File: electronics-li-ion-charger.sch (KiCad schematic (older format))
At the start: 16 parts, among them J1 Conn_01x01_Male, J2 Conn_01x01_Male, J3 USB_B_Micro, J4 Conn_01x03_Male, U1 MCP73831-2-OT

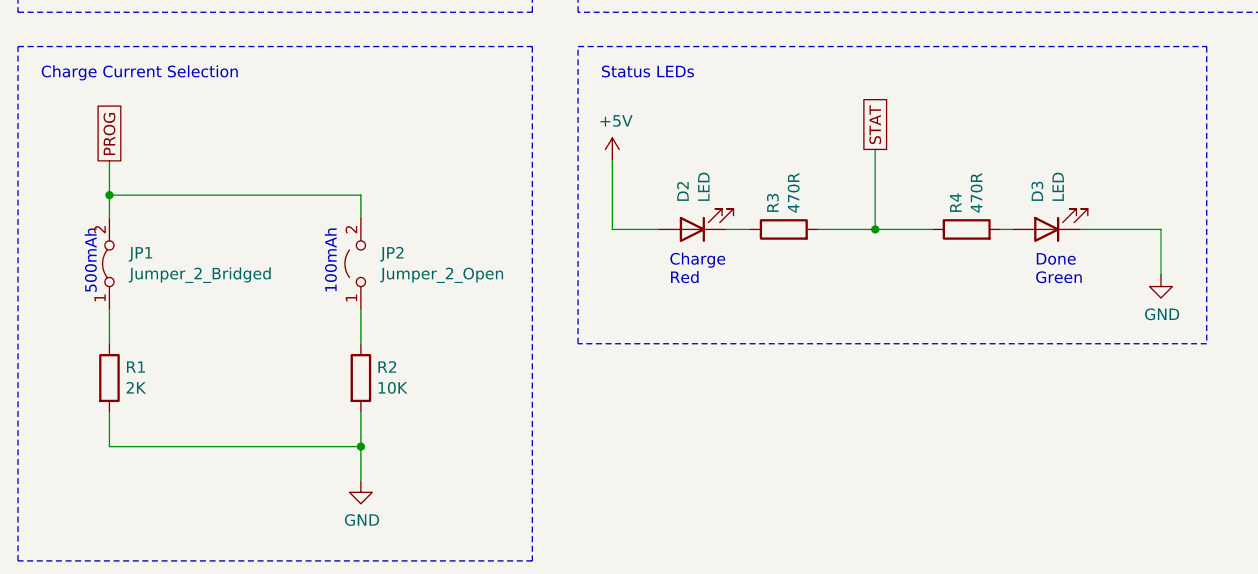
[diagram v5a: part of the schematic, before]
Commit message: Place components in PCB layout.
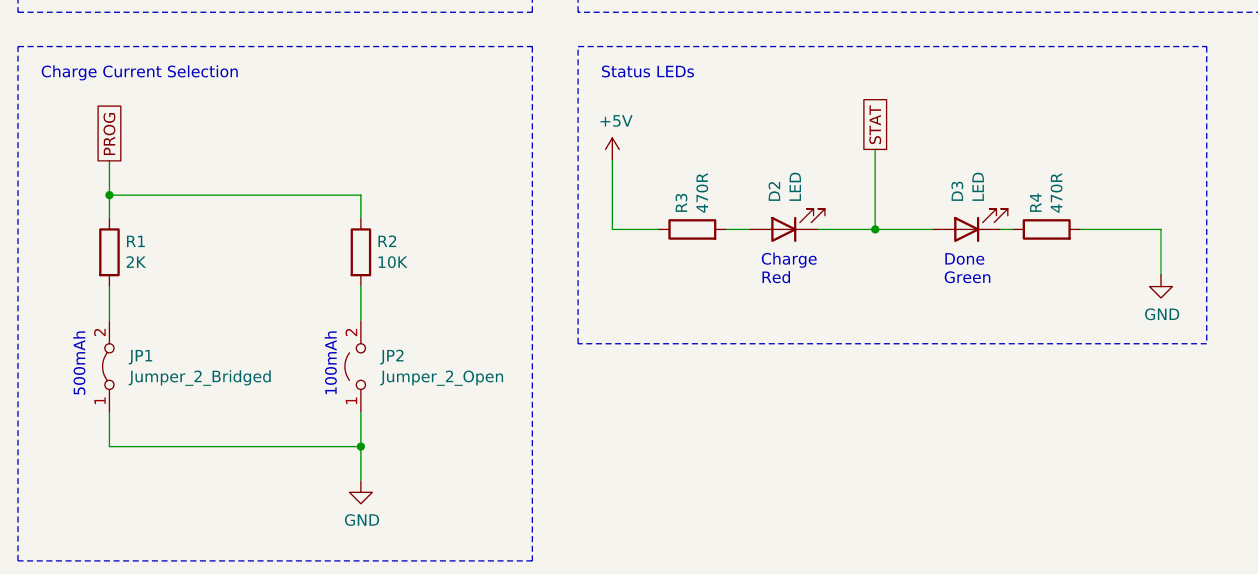
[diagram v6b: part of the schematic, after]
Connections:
- net +5V: now also R3.1; no longer D2.2 (A)
- net GND: now also JP1.1 (A), JP2.1 (A), R4.2; no longer D3.1 (K), R1.2, R2.2
- net PROG: now also R1.1, R2.1; no longer JP1.2 (B), JP2.2 (B)
- net STAT: now also D2.1 (K), D3.2 (A); no longer R3.2, R4.1
- new net: D3.1 (K), R4.1
- new net: D2.2 (A), R3.2
- new net: JP2.2 (B), R2.2
- new net: JP1.2 (B), R1.2
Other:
- moved on the sheet: D2, D3, JP1, JP2, R1, R2, R3, R4
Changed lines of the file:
@@
 L Device:R R4
 U 1 1 5FFB4EF8
-P 6800 4950
-F 0 "R4" H 6870 4996 50  0000 L CNN
-F 1 "470R" H 6870 4905 50  0000 L CNN
-F 2 "Resistor_SMD:R_1206_3216Metric_Pad1.30x1.75mm_HandSolder" V 6730 4950 50  0001 C CNN
-F 3 "~" H 6800 4950 50  0001 C CNN
-	1    6800 4950
+P 7150 4950
+F 0 "R4" H 7220 4996 50  0000 L CNN
+F 1 "470R" H 7220 4905 50  0000 L CNN
+F 2 "Resistor_SMD:R_1206_3216Metric_Pad1.30x1.75mm_HandSolder" V 7080 4950 50  0001 C CNN
+F 3 "~" H 7150 4950 50  0001 C CNN
+	1    7150 4950
 	0    -1   -1   0
 $EndComp
@@
 L Device:R R3
 U 1 1 5FFB5567
-P 6000 4950
-F 0 "R3" H 6070 4996 50  0000 L CNN
-F 1 "470R" H 6070 4905 50  0000 L CNN
-F 2 "Resistor_SMD:R_1206_3216Metric_Pad1.30x1.75mm_HandSolder" V 5930 4950 50  0001 C CNN
-F 3 "~" H 6000 4950 50  0001 C CNN
-	1    6000 4950
+P 5600 4950
+F 0 "R3" H 5670 4996 50  0000 L CNN
+F 1 "470R" H 5670 4905 50  0000 L CNN
+F 2 "Resistor_SMD:R_1206_3216Metric_Pad1.30x1.75mm_HandSolder" V 5530 4950 50  0001 C CNN
+F 3 "~" H 5600 4950 50  0001 C CNN
+	1    5600 4950
 	0    -1   -1   0
 $EndComp
@@
 L Device:LED D3
 U 1 1 5FFB6F7B
-P 7150 4950
-F 0 "D3" V 7189 4832 50  0000 R CNN
-F 1 "LED" V 7098 4832 50  0000 R CNN
-F 2 "LED_SMD:LED_1206_3216Metric_Pad1.42x1.75mm_HandSolder" H 7150 4950 50  0001 C CNN
-F 3 "~" H 7150 4950 50  0001 C CNN
-	1    7150 4950
+P 6800 4950
+F 0 "D3" V 6839 4832 50  0000 R CNN
+F 1 "LED" V 6748 4832 50  0000 R CNN
+F 2 "LED_SMD:LED_1206_3216Metric_Pad1.42x1.75mm_HandSolder" H 6800 4950 50  0001 C CNN
+F 3 "~" H 6800 4950 50  0001 C CNN
+	1    6800 4950
 	-1   0    0    1
 $EndComp
@@
 L Device:LED D2
 U 1 1 5FFB7C3E
-P 5600 4950
-F 0 "D2" V 5639 4832 50  0000 R CNN
-F 1 "LED" V 5548 4832 50  0000 R CNN
-F 2 "LED_SMD:LED_1206_3216Metric_Pad1.42x1.75mm_HandSolder" H 5600 4950 50  0001 C CNN
-F 3 "~" H 5600 4950 50  0001 C CNN
-	1    5600 4950
+P 6000 4950
+F 0 "D2" V 6039 4832 50  0000 R CNN
+F 1 "LED" V 5948 4832 50  0000 R CNN
+F 2 "LED_SMD:LED_1206_3216Metric_Pad1.42x1.75mm_HandSolder" H 6000 4950 50  0001 C CNN
+F 3 "~" H 6000 4950 50  0001 C CNN
+	1    6000 4950
 	-1   0    0    1
 $EndComp
@@
 L Device:R R2
 U 1 1 5FFB5769
-P 4150 5600
-F 0 "R2" H 4220 5646 50  0000 L CNN
-F 1 "10K" H 4220 5555 50  0000 L CNN
-F 2 "Resistor_SMD:R_1206_3216Metric_Pad1.30x1.75mm_HandSolder" V 4080 5600 50  0001 C CNN
-F 3 "~" H 4150 5600 50  0001 C CNN
-	1    4150 5600
+P 4150 5050
+F 0 "R2" H 4220 5096 50  0000 L CNN
+F 1 "10K" H 4220 5005 50  0000 L CNN
+F 2 "Resistor_SMD:R_1206_3216Metric_Pad1.30x1.75mm_HandSolder" V 4080 5050 50  0001 C CNN
+F 3 "~" H 4150 5050 50  0001 C CNN
+	1    4150 5050
 	1    0    0    -1
 $EndComp
@@
 L Jumper:Jumper_2_Bridged JP1
 U 1 1 5FFBEBFA
-P 3050 5100
-F 0 "JP1" V 3096 5012 50  0000 R CNN
-F 1 "Jumper_2_Bridged" V 3005 5012 50  0000 R CNN
-F 2 "Connector_PinHeader_2.54mm:PinHeader_1x02_P2.54mm_Vertical" H 3050 5100 50  0001 C CNN
-F 3 "~" H 3050 5100 50  0001 C CNN
-	1    3050 5100
+P 3050 5550
+F 0 "JP1" V 3096 5462 50  0000 R CNN
+F 1 "Jumper_2_Bridged" V 3005 5462 50  0000 R CNN
+F 2 "Connector_PinHeader_2.54mm:PinHeader_1x02_P2.54mm_Vertical" H 3050 5550 50  0001 C CNN
+F 3 "~" H 3050 5550 50  0001 C CNN
+	1    3050 5550
 	0    -1   -1   0
 $EndComp
@@
 L Device:R R1
 U 1 1 5FFB5B83
-P 3050 5600
-F 0 "R1" H 3120 5646 50  0000 L CNN
-F 1 "2K" H 3120 5555 50  0000 L CNN
-F 2 "Resistor_SMD:R_1206_3216Metric_Pad1.30x1.75mm_HandSolder" V 2980 5600 50  0001 C CNN
-F 3 "~" H 3050 5600 50  0001 C CNN
-	1    3050 5600
+P 3050 5050
+F 0 "R1" H 3120 5096 50  0000 L CNN
+F 1 "2K" H 3120 5005 50  0000 L CNN
+F 2 "Resistor_SMD:R_1206_3216Metric_Pad1.30x1.75mm_HandSolder" V 2980 5050 50  0001 C CNN
+F 3 "~" H 3050 5050 50  0001 C CNN
+	1    3050 5050
 	1    0    0    -1
 $EndComp
@@
 	4150 4800 4150 4900
 Wire Wire Line
-	3050 5300 3050 5450
-Wire Wire Line
-	4150 5300 4150 5450
-Wire Wire Line
 	4150 6050 4150 5900
 Wire Wire Line
@@
 L Jumper:Jumper_2_Open JP2
 U 1 1 5FFBE0EB
-P 4150 5100
-F 0 "JP2" V 4196 5012 50  0000 R CNN
-F 1 "Jumper_2_Open" V 4105 5012 50  0000 R CNN
-F 2 "Connector_PinHeader_2.54mm:PinHeader_1x02_P2.54mm_Vertical" H 4150 5100 50  0001 C CNN
-F 3 "~" H 4150 5100 50  0001 C CNN
-	1    4150 5100
+P 4150 5550
+F 0 "JP2" V 4196 5462 50  0000 R CNN
+F 1 "Jumper_2_Open" V 4105 5462 50  0000 R CNN
+F 2 "Connector_PinHeader_2.54mm:PinHeader_1x02_P2.54mm_Vertical" H 4150 5550 50  0001 C CNN
+F 3 "~" H 4150 5550 50  0001 C CNN
+	1    4150 5550
 	0    -1   -1   0
 $EndComp
@@
 Wire Wire Line
 	5250 4950 5450 4950
-Text Notes 3000 4950 3    50   ~ 0
+Text Notes 2950 5400 3    50   ~ 0
 500mAh
-Text Notes 4050 4950 3    50   ~ 0
+Text Notes 4050 5400 3    50   ~ 0
 100mAh
 Wire Wire Line
@@
 Text Notes 5200 4300 0    50   ~ 0
 Status LEDs
-Text Notes 5500 5200 0    50   ~ 0
+Text Notes 5900 5200 0    50   ~ 0
 Charge\nRed
-Text Notes 7100 5200 0    50   ~ 0
+Text Notes 6700 5200 0    50   ~ 0
 Done\nGreen
 Wire Notes Line
@@
 Text Label 6850 3100 0    50   ~ 0
 VBAT
+Wire Wire Line
+	3050 5200 3050 5350
+Wire Wire Line
+	4150 5200 4150 5350
 $EndSCHEMATC
